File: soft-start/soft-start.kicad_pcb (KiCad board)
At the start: 2 copper layers, 17 parts, among them M1 Motor_DC, Q1 IRFB3004PbF, SW1 SW_SPST_Temperature, U1 TLC555xP

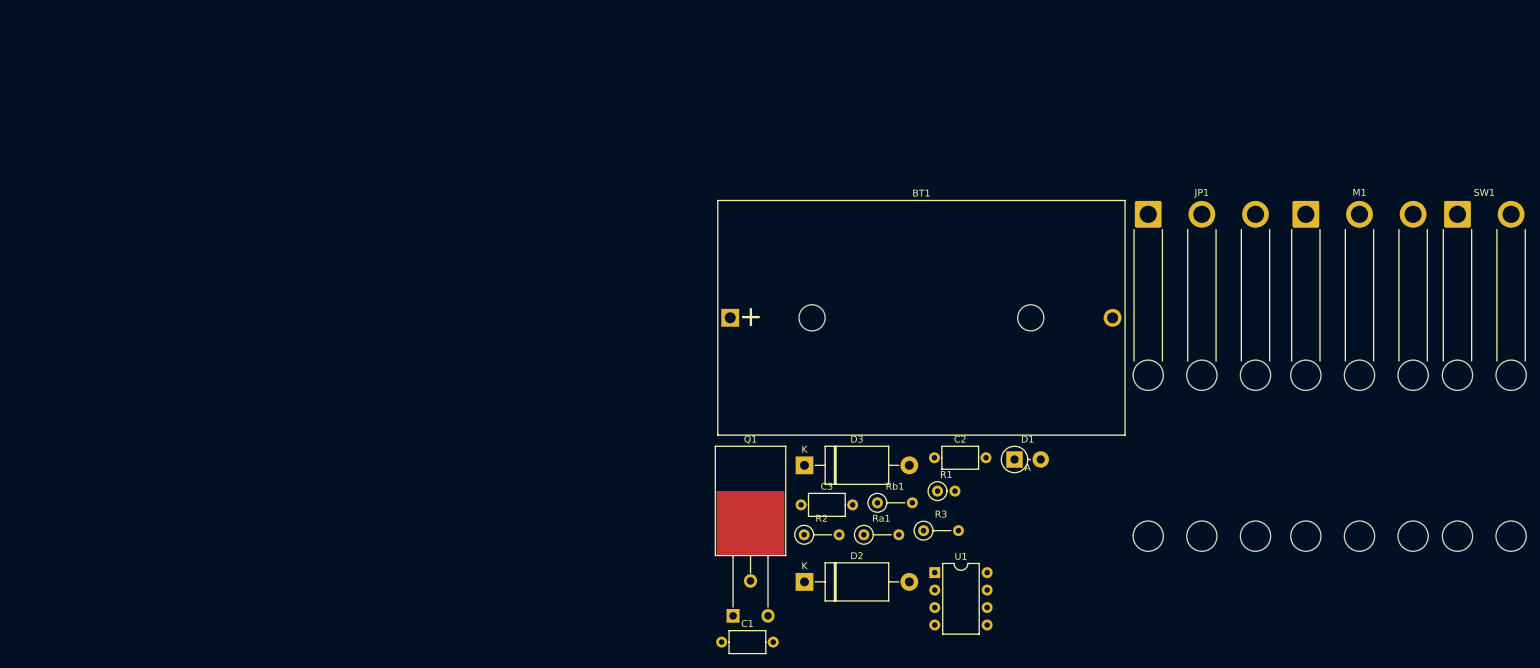
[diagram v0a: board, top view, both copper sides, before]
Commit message: [soft-start] Add PCB
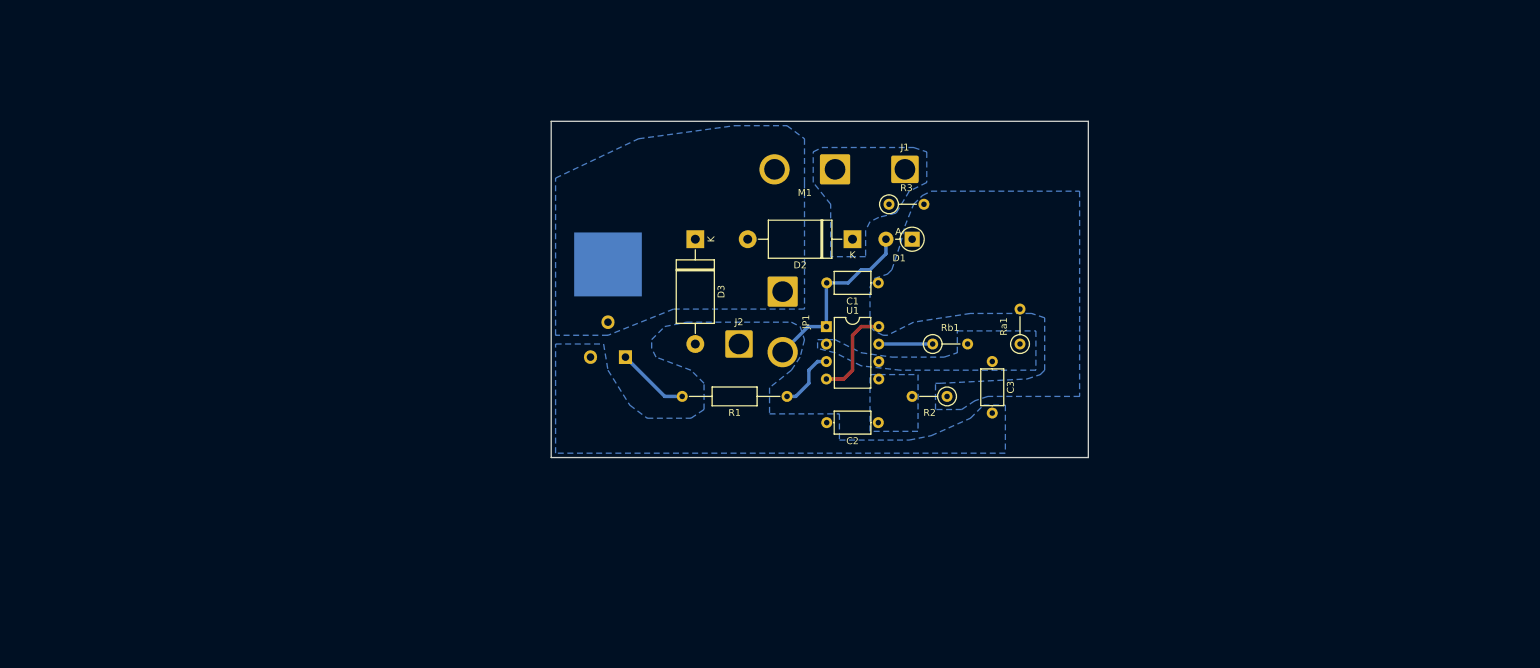
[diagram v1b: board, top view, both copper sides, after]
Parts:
- removed BT1: 14V, Battery:BatteryHolder_Bulgin_BX0036_1xC
- removed SW1: SW_SPST_Temperature, Connector_Wire:SolderWire-2sqmm_1x02_P7.8mm_D2mm_OD3.9mm_Relief2x
- added J1: Conn_01x01_Female, Connector_Wire:SolderWire-2.5sqmm_1x01_D2.4mm_OD3.6mm, F.Cu at (203.2, 69.8)
- added J2: Conn_01x01_Female, Connector_Wire:SolderWire-2.5sqmm_1x01_D2.4mm_OD3.6mm, F.Cu at (179.1, 95.2)
- D1: footprint Diode_THT:D_DO-15_P3.81mm_Vertical_AnodeUp -> Diode_THT:D_DO-41_SOD81_P3.81mm_Vertical_AnodeUp
- JP1, M1: footprint Connector_Wire:SolderWire-2sqmm_1x03_P7.8mm_D2mm_OD3.9mm_Relief2x -> Connector_Wire:SolderWire-2.5sqmm_1x02_P8.8mm_D2.4mm_OD4.4mm
- Q1: moved to B.Cu
- R1: footprint Resistor_THT:R_Axial_DIN0207_L6.3mm_D2.5mm_P2.54mm_Vertical -> Resistor_THT:R_Axial_DIN0207_L6.3mm_D2.5mm_P15.24mm_Horizontal
- moved M1 68.8 mm to (193.0, 69.8), turned to 180 degrees
- moved C1 57.0 mm to (199.3, 86.4), turned to 180 degrees
- moved JP1 54.3 mm to (185.4, 87.6), turned to -90 degrees
- moved D2 50.3 mm to (195.6, 80.0), turned to 180 degrees
- moved R3 47.7 mm to (200.9, 74.9)
- moved Q1 40.8 mm to (162.6, 92.1), turned to 180 degrees
- moved U1 39.1 mm to (191.8, 92.7)
- moved D3 36.5 mm to (172.7, 80.0), turned to -90 degrees
- moved Ra1 35.8 mm to (219.9, 95.2), turned to 90 degrees
- moved D1 35.3 mm to (204.3, 80.0), turned to 180 degrees
- moved C3 34.8 mm to (215.9, 97.8), turned to -90 degrees
- moved R2 28.9 mm to (209.3, 102.9), turned to 180 degrees
- moved R1 25.9 mm to (186.1, 102.9), turned to 180 degrees
- moved Rb1 24.4 mm to (207.2, 95.2)
- moved C2 9.63 mm to (199.3, 106.7), turned to 180 degrees
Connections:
- D1 pad 1: VCC -> VDD
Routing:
- net GND: track 0.00 -> 26.8 mm
- net VDD: track 0.00 -> 13.8 mm
- net /PWM: track 0.00 -> 10.6 mm
- net Net-(R1-Pad1): track 0.00 -> 8.95 mm
- net Net-(Rb1-Pad1): track 0.00 -> 7.87 mm
- added copper zone on B.Cu, net GND
- added copper zone on B.Cu, net Net-(C2-Pad1)
- added copper zone on B.Cu, net Net-(C3-Pad1)
- added copper zone on B.Cu, net Net-(D2-Pad2)
- added copper zone on B.Cu, net VCC
- added copper zone on B.Cu, net VDD
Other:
- board outline added: 78.1 x 48.9 mm

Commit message: [soft-start] Small changes
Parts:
- moved J2 25.8 mm to (156.2, 107.3)
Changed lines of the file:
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@@
   )
   (footprint "Connector_Wire:SolderWire-2.5sqmm_1x01_D2.4mm_OD3.6mm" (layer "F.Cu")
-    (at 179.07 95.25)
+    (at 156.21 107.315)
     (descr "Soldered wire connection, for a single 2.5 mm² wire, basic insulation, conductor diameter 2.4mm, outer diameter 3.6mm, size source Multi-Contact FLEXI-E 2.5 (https://ec.staubli.com/AcroFiles/Catalogues/TM_Cab-Main-11014119_(en)_hi.pdf), bend radius 3 times outer diameter, generated with kicad-footprint-generator")
     (tags "connector wire 2.5sqmm")
@@
   (segment (start 190.5 97.79) (end 189.23 99.06) (width 0.5) (layer "B.Cu") (net 8))
   (segment (start 191.78 97.8) (end 190.51 97.8) (width 0.5) (layer "B.Cu") (net 8))
-  (segment (start 199.41 95.25) (end 199.4 95.26) (width 0.5) (layer "B.Cu") (net 9))
-  (segment (start 199.4 95.26) (end 199.39 95.25) (width 0.5) (layer "B.Cu") (net 9))
+  (segment (start 199.4 95.26) (end 207.225 95.26) (width 0.5) (layer "B.Cu") (net 9))
   (segment (start 207.225 95.26) (end 207.235 95.25) (width 0.5) (layer "B.Cu") (net 9))
-  (segment (start 207.235 95.25) (end 199.41 95.25) (width 0.5) (layer "B.Cu") (net 9))
   (zone (net 6) (net_name "Net-(D2-Pad2)") (layer "B.Cu") (hatch edge 0.508)
-    (connect_pads (clearance 0.508))
+    (connect_pads yes (clearance 0.508))
     (min_thickness 0.254) (filled_areas_thickness no)
     (fill yes (thermal_gap 0.508) (thermal_bridge_width 0.508))
@@
   )
   (zone (net 5) (net_name "VCC") (layer "B.Cu") (hatch edge 0.508)
-    (connect_pads (clearance 0.508))
+    (connect_pads yes (clearance 0.508))
     (min_thickness 0.254) (filled_areas_thickness no)
     (fill yes (thermal_gap 0.508) (thermal_bridge_width 0.508))

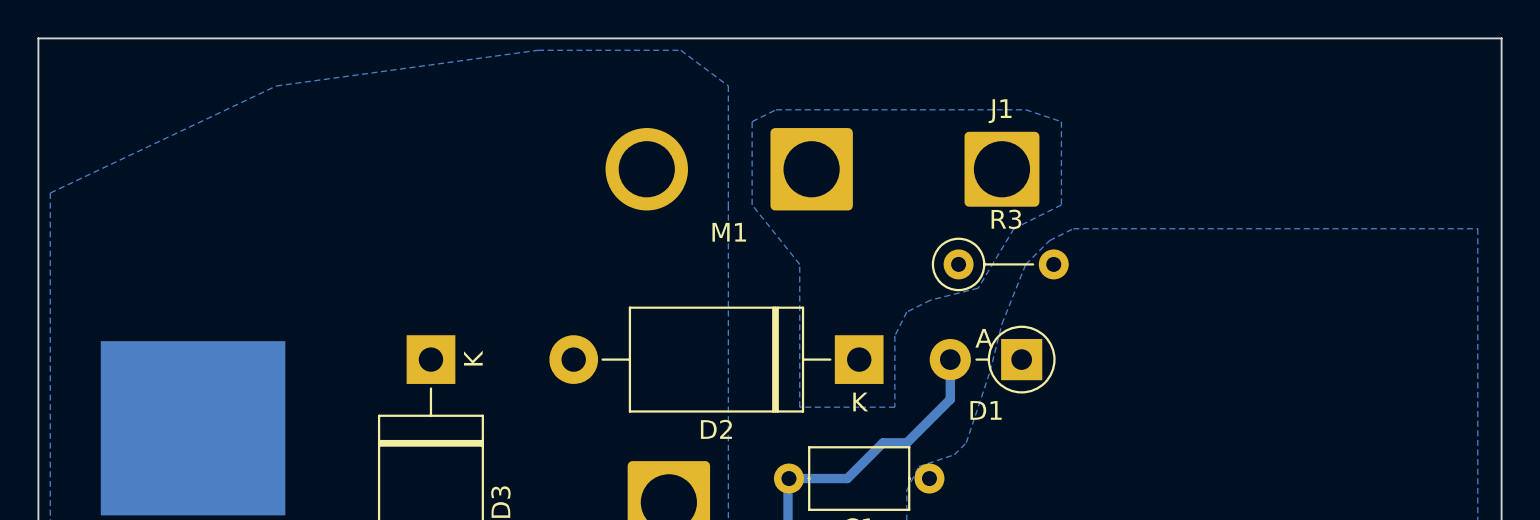
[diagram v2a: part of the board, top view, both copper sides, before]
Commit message: [diag] Add cooler working diagnostic schematic
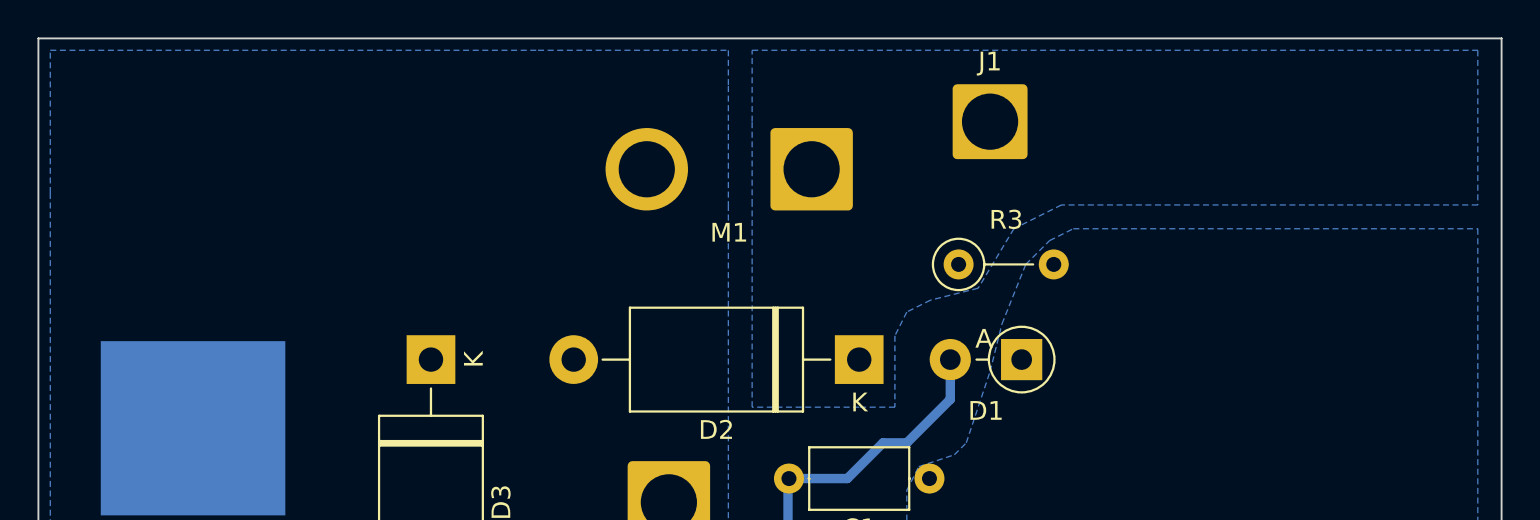
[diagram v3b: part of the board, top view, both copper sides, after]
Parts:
- moved J1 2.62 mm to (202.6, 67.3)
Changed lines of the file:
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@@
   )
   (footprint "Connector_Wire:SolderWire-2.5sqmm_1x01_D2.4mm_OD3.6mm" (layer "F.Cu")
-    (at 203.2 69.85)
+    (at 202.565 67.31)
     (descr "Soldered wire connection, for a single 2.5 mm² wire, basic insulation, conductor diameter 2.4mm, outer diameter 3.6mm, size source Multi-Contact FLEXI-E 2.5 (https://ec.staubli.com/AcroFiles/Catalogues/TM_Cab-Main-11014119_(en)_hi.pdf), bend radius 3 times outer diameter, generated with kicad-footprint-generator")
     (tags "connector wire 2.5sqmm")
@@
         (xy 152.4 93.98)
         (xy 152.4 71.12)
-        (xy 164.465 65.405)
+        (xy 152.4 63.5)
         (xy 178.435 63.5)
-        (xy 186.055 63.5)
+        (xy 188.595 63.5)
       )
     )
@@
     (polygon
       (pts
-        (xy 206.375 67.31)
+        (xy 228.6 71.755)
         (xy 206.375 71.755)
         (xy 203.835 73.025)
@@
         (xy 197.485 82.55)
         (xy 195.58 82.55)
-        (xy 192.405 82.55)
-        (xy 192.405 74.93)
+        (xy 189.865 82.55)
+        (xy 189.865 74.93)
         (xy 189.865 71.755)
         (xy 189.865 67.31)
-        (xy 191.135 66.675)
-        (xy 204.47 66.675)
-      )
-    )
+        (xy 189.865 63.5)
+        (xy 228.6 63.5)
+      )
+    )

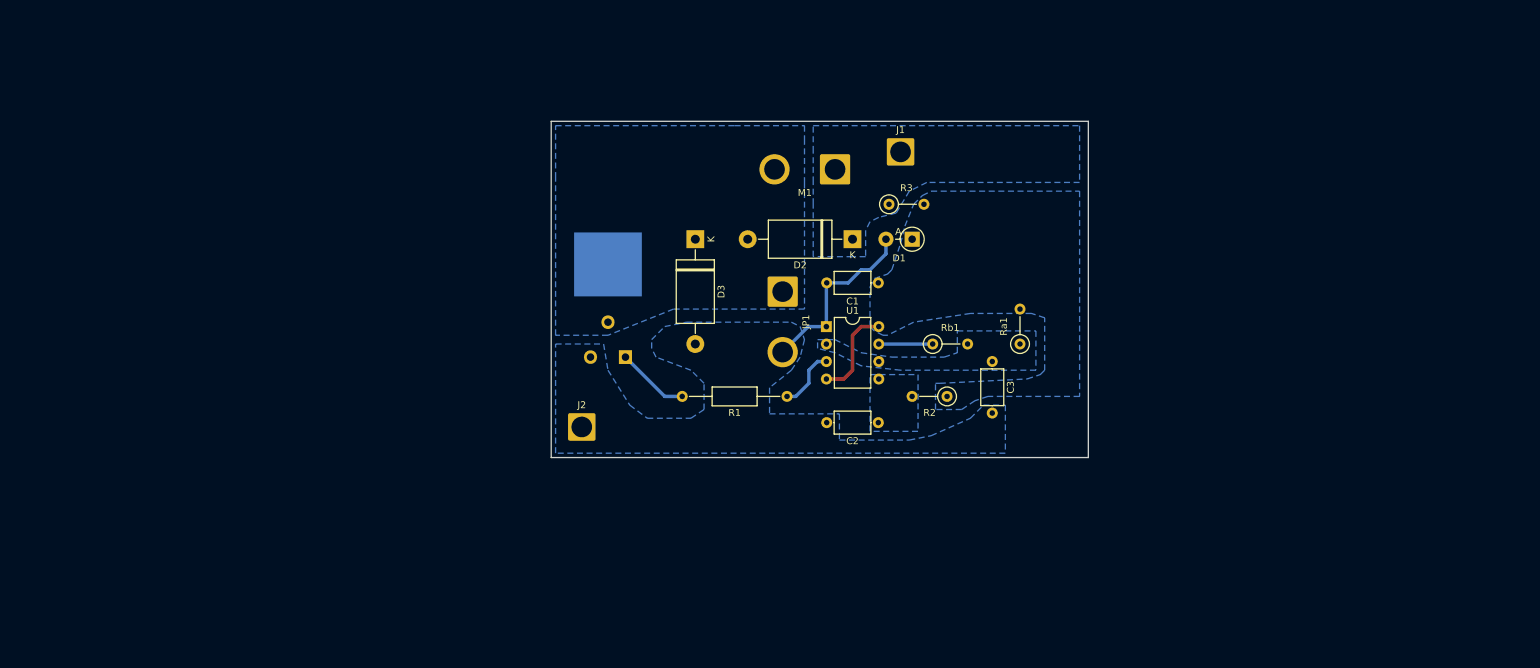
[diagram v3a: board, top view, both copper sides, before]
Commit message: [soft-start] Update to use counter as time delay source
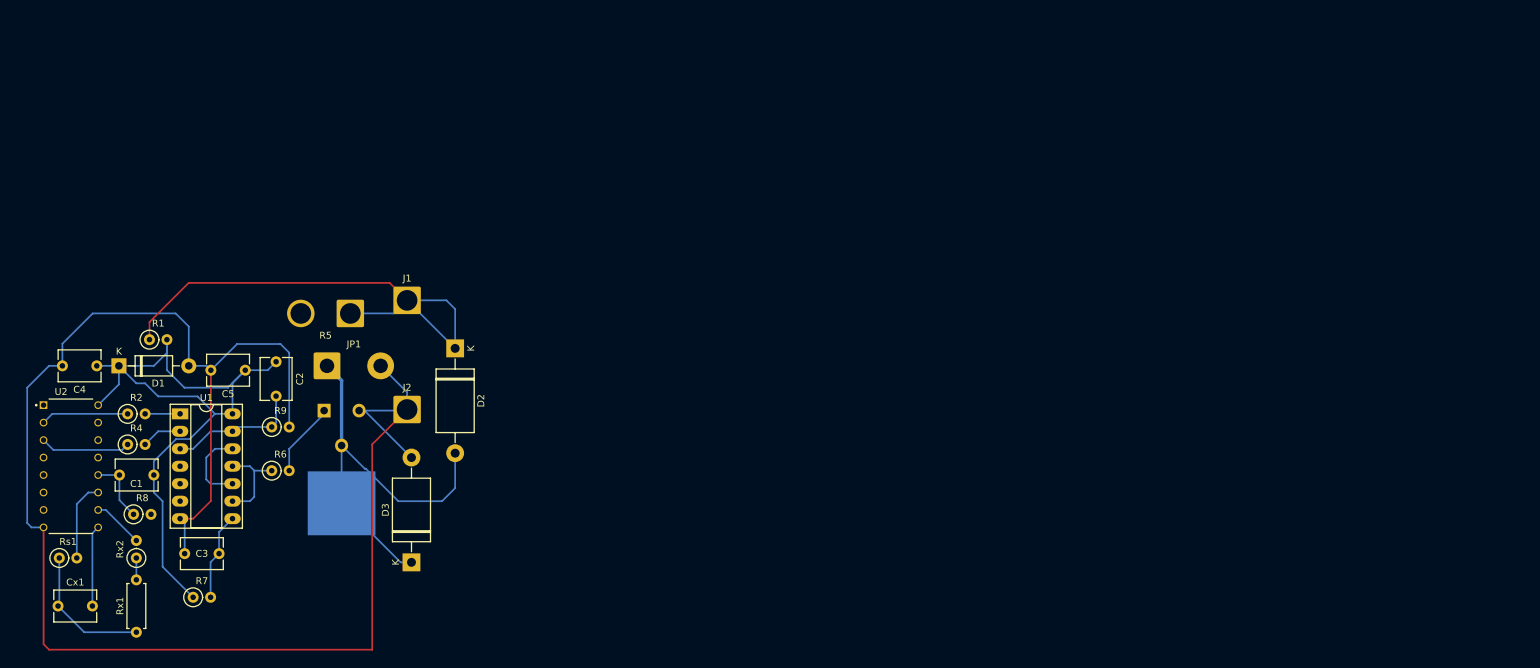
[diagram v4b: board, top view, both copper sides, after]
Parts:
- removed M1: Motor_DC, Connector_Wire:SolderWire-2.5sqmm_1x02_P8.8mm_D2.4mm_OD4.4mm
- removed R3: R, Resistor_THT:R_Axial_DIN0207_L6.3mm_D2.5mm_P5.08mm_Vertical
- removed Ra1: 100k, Resistor_THT:R_Axial_DIN0207_L6.3mm_D2.5mm_P5.08mm_Vertical
- removed Rb1: 10k, Resistor_THT:R_Axial_DIN0207_L6.3mm_D2.5mm_P5.08mm_Vertical
- added C4: C, Capacitor_THT:C_Disc_D6.0mm_W4.4mm_P5.00mm, F.Cu at (85.7, 98.4)
- added C5: C, Capacitor_THT:C_Disc_D6.0mm_W4.4mm_P5.00mm, F.Cu at (107.3, 99.1)
- added Cx1: 11nF, Capacitor_THT:C_Disc_D6.0mm_W4.4mm_P5.00mm, F.Cu at (80.0, 133.3)
- added R4: 51k, Resistor_THT:R_Axial_DIN0207_L6.3mm_D2.5mm_P2.54mm_Vertical, F.Cu at (90.2, 109.9)
- added R5: 0.18, 25W?, Connector_Wire:SolderWire-2.5sqmm_1x02_P7.2mm_D2.4mm_OD3.6mm, F.Cu at (122.6, 90.8)
- added R6: 100 .. 1k, Resistor_THT:R_Axial_DIN0207_L6.3mm_D2.5mm_P2.54mm_Vertical, F.Cu at (111.1, 113.7)
- added R7: R, Resistor_THT:R_Axial_DIN0207_L6.3mm_D2.5mm_P2.54mm_Vertical, F.Cu at (99.7, 132.1)
- added R8: R, Resistor_THT:R_Axial_DIN0207_L6.3mm_D2.5mm_P2.54mm_Vertical, F.Cu at (91.0, 120.0)
- added R9: R, Resistor_THT:R_Axial_DIN0207_L6.3mm_D2.5mm_P2.54mm_Vertical, F.Cu at (111.1, 107.3)
- added Rs1: (2..10) * Rx, Resistor_THT:R_Axial_DIN0207_L6.3mm_D2.5mm_P2.54mm_Vertical, F.Cu at (80.2, 126.4)
- added Rx1: 6.8k, Resistor_THT:R_Axial_DIN0207_L6.3mm_D2.5mm_P7.62mm_Horizontal, F.Cu at (91.4, 137.2)
- added Rx2: 3.3k, Resistor_THT:R_Axial_DIN0207_L6.3mm_D2.5mm_P2.54mm_Vertical, F.Cu at (91.4, 126.4)
- added U2: CD4060BE, LIB:DIP794W45P254L1969H508Q16, F.Cu at (81.9, 113.0)
- C1: value 100u -> C; footprint Capacitor_THT:C_Axial_L5.1mm_D3.1mm_P7.50mm_Horizontal -> Capacitor_THT:C_Disc_D6.0mm_W4.4mm_P5.00mm
- C2: value 150n -> C; footprint Capacitor_THT:C_Axial_L5.1mm_D3.1mm_P7.50mm_Horizontal -> Capacitor_THT:C_Disc_D6.0mm_W4.4mm_P5.00mm
- C3: value 22n -> C; footprint Capacitor_THT:C_Axial_L5.1mm_D3.1mm_P7.50mm_Horizontal -> Capacitor_THT:C_Disc_D6.0mm_W4.4mm_P5.00mm
- D1: value D_Zener -> 1N4740A; footprint Diode_THT:D_DO-41_SOD81_P3.81mm_Vertical_AnodeUp -> Diode_THT:D_DO-41_SOD81_P10.16mm_Horizontal
- J1, J2: value Conn_01x01_Female -> ~
- JP1: footprint Connector_Wire:SolderWire-2.5sqmm_1x02_P8.8mm_D2.4mm_OD4.4mm -> Connector_Wire:SolderWire-1.5sqmm_1x02_P7.8mm_D1.7mm_OD3.9mm
- R1: value 100 -> 150, 0.25W; footprint Resistor_THT:R_Axial_DIN0207_L6.3mm_D2.5mm_P15.24mm_Horizontal -> Resistor_THT:R_Axial_DIN0207_L6.3mm_D2.5mm_P2.54mm_Vertical
- R2: value 2k -> 51k; footprint Resistor_THT:R_Axial_DIN0207_L6.3mm_D2.5mm_P5.08mm_Vertical -> Resistor_THT:R_Axial_DIN0207_L6.3mm_D2.5mm_P2.54mm_Vertical
- U1: value TLC555xP -> 4011; footprint Package_DIP:DIP-8_W7.62mm -> Package_DIP:DIP-14_W7.62mm_Socket_LongPads
- moved R2 119.2 mm to (90.2, 105.4), turned to 0 degrees
- moved D1 116.8 mm to (88.9, 98.4), turned to 0 degrees
- moved C3 115.9 mm to (103.5, 125.7), turned to 180 degrees
- moved C1 109.0 mm to (94.0, 114.3)
- moved U1 94.8 mm to (97.8, 105.4)
- moved R1 93.1 mm to (93.3, 94.6), turned to 0 degrees
- moved C2 88.0 mm to (111.8, 97.8), turned to -90 degrees
- moved J1 74.9 mm to (130.8, 88.9)
- moved JP1 67.1 mm to (119.2, 98.4), turned to 0 degrees
- moved D3 62.5 mm to (131.4, 127.0), turned to 90 degrees
- moved D2 59.9 mm to (137.8, 95.9), turned to -90 degrees
- moved Q1 47.3 mm to (118.7, 110.0), turned to 0 degrees
- moved J2 25.5 mm to (130.8, 104.8)
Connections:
- C1 pad 1: VDD -> VCC
- C1 pad 2: GND -> /COUNTER_RESET
- C2 pad 1: Net-(C2-Pad1) -> VCC
- C2 pad 2: GND -> /TRIGGER_SET
- C3 pad 1: Net-(C3-Pad1) -> /TRIGGER_RESET
- D1 pad 1: VDD -> VCC
- D2 pad 1: VCC -> +BATT
- J1 pad 1: VCC -> +BATT
- Q1 pad 1: /PWM -> Net-(Q1-G)
- R1 pad 1: Net-(R1-Pad1) -> +BATT
- R1 pad 2: /PWM -> VCC
- R2 pad 1: VDD -> Net-(U2-Q13)
- R2 pad 2: Net-(C2-Pad1) -> Net-(R2-Pad2)
- U1 pad 1: GND -> Net-(R2-Pad2)
- U1 pad 2: Net-(C3-Pad1) -> Net-(R4-Pad2)
- U1 pad 3: Net-(R1-Pad1) -> /TRIGGER_SET
- U1 pad 4: VDD -> unconnected-(U1-Pad4)
- U1 pad 5: Net-(C2-Pad1) -> unconnected-(U1-Pad5)
- U1 pad 6: Net-(C3-Pad1) -> unconnected-(U1-Pad6)
- U1 pad 7: Net-(Rb1-Pad1) -> GND
- U1 pad 8: VDD -> /TRIGGER_RESET
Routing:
- net GND: track 26.8 -> 244.8 mm
- net VCC: track 0.00 -> 103.2 mm
- net +BATT: track 0.00 -> 75.6 mm
- net Net-(D2-A2): track 0.00 -> 63.6 mm
- net Net-(Cx1-Pad1): track 0.00 -> 20.0 mm
- net /TRIGGER_SET: track 0.00 -> 19.4 mm
- net VDD: track 13.8 -> 0.00 mm
- net /TRIGGER_OUT: track 0.00 -> 13.2 mm
- net Net-(U2-Q14): track 0.00 -> 13.2 mm
- net /TRIGGER_RESET: track 0.00 -> 12.8 mm
- net Net-(U2-Q13): track 0.00 -> 12.8 mm
- net Net-(U2-(PHI)O): track 0.00 -> 11.8 mm
- net Net-(U2-(PHI)I): track 0.00 -> 11.7 mm
- net Net-(U1-Pad10): track 0.00 -> 11.6 mm
- net Net-(Q1-G): track 0.00 -> 10.8 mm
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- removed copper zone on B.Cu, net GND
- removed copper zone on B.Cu, net Net-(C2-Pad1)
- removed copper zone on B.Cu, net Net-(C3-Pad1)
- removed copper zone on B.Cu, net Net-(D2-A2)
- removed copper zone on B.Cu, net VCC
- removed copper zone on B.Cu, net VDD
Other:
- board outline removed
